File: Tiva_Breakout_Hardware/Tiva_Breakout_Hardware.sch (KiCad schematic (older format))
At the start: 54 parts, among them U1 TM4C129E_Launchpad

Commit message: Finished all wiring and LEDs, need resizing and silkscreen
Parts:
- gave numbers to parts that had none: 20
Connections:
- net PATCH10_EN: now also ConnPCH_C2.2 (Pin_2), R15.2, U1.PF1 (C1_1); no longer ConnPCH_C2.1 (Pin_1), R24.2, U1.PL3 (C1_10)
- net PATCH1_EN: now also ConnPCH_C2.1 (Pin_1), R24.2, U1.PL3 (C1_10); no longer ConnPCH_C2.2 (Pin_2), R15.2, U1.PF1 (C1_1)
- net PATCH2_EN: now also ConnPCH_C2.3 (Pin_3), R23.2, U1.PL2 (C1_9); no longer ConnPCH_C2.4 (Pin_4), R16.2, U1.PF2 (C1_2)
- net PATCH3_EN: now also ConnPCH_C2.5 (Pin_5), R22.2, U1.PL1 (C1_8); no longer ConnPCH_C2.6 (Pin_6), R17.2, U1.PF3 (C1_3)
- net PATCH4_EN: now also ConnPCH_C2.7 (Pin_7), R21.2, U1.PL0 (C1_7); no longer ConnPCH_C2.8 (Pin_8), R18.2, U1.PG0 (C1_4)
- net PATCH5_EN: now also ConnPCH_C2.9 (Pin_9), R20.2, U1.PL5 (C1_6); no longer ConnPCH_C2.10 (Pin_10), R19.2, U1.PL4 (C1_5)
- net PATCH6_EN: now also ConnPCH_C2.10 (Pin_10), R19.2, U1.PL4 (C1_5); no longer ConnPCH_C2.9 (Pin_9), R20.2, U1.PL5 (C1_6)
- net PATCH7_EN: now also ConnPCH_C2.8 (Pin_8), R18.2, U1.PG0 (C1_4); no longer ConnPCH_C2.7 (Pin_7), R21.2, U1.PL0 (C1_7)
- net PATCH8_EN: now also ConnPCH_C2.6 (Pin_6), R17.2, U1.PF3 (C1_3); no longer ConnPCH_C2.5 (Pin_5), R22.2, U1.PL1 (C1_8)
- net PATCH9_EN: now also ConnPCH_C2.4 (Pin_4), R16.2, U1.PF2 (C1_2); no longer ConnPCH_C2.3 (Pin_3), R23.2, U1.PL2 (C1_9)

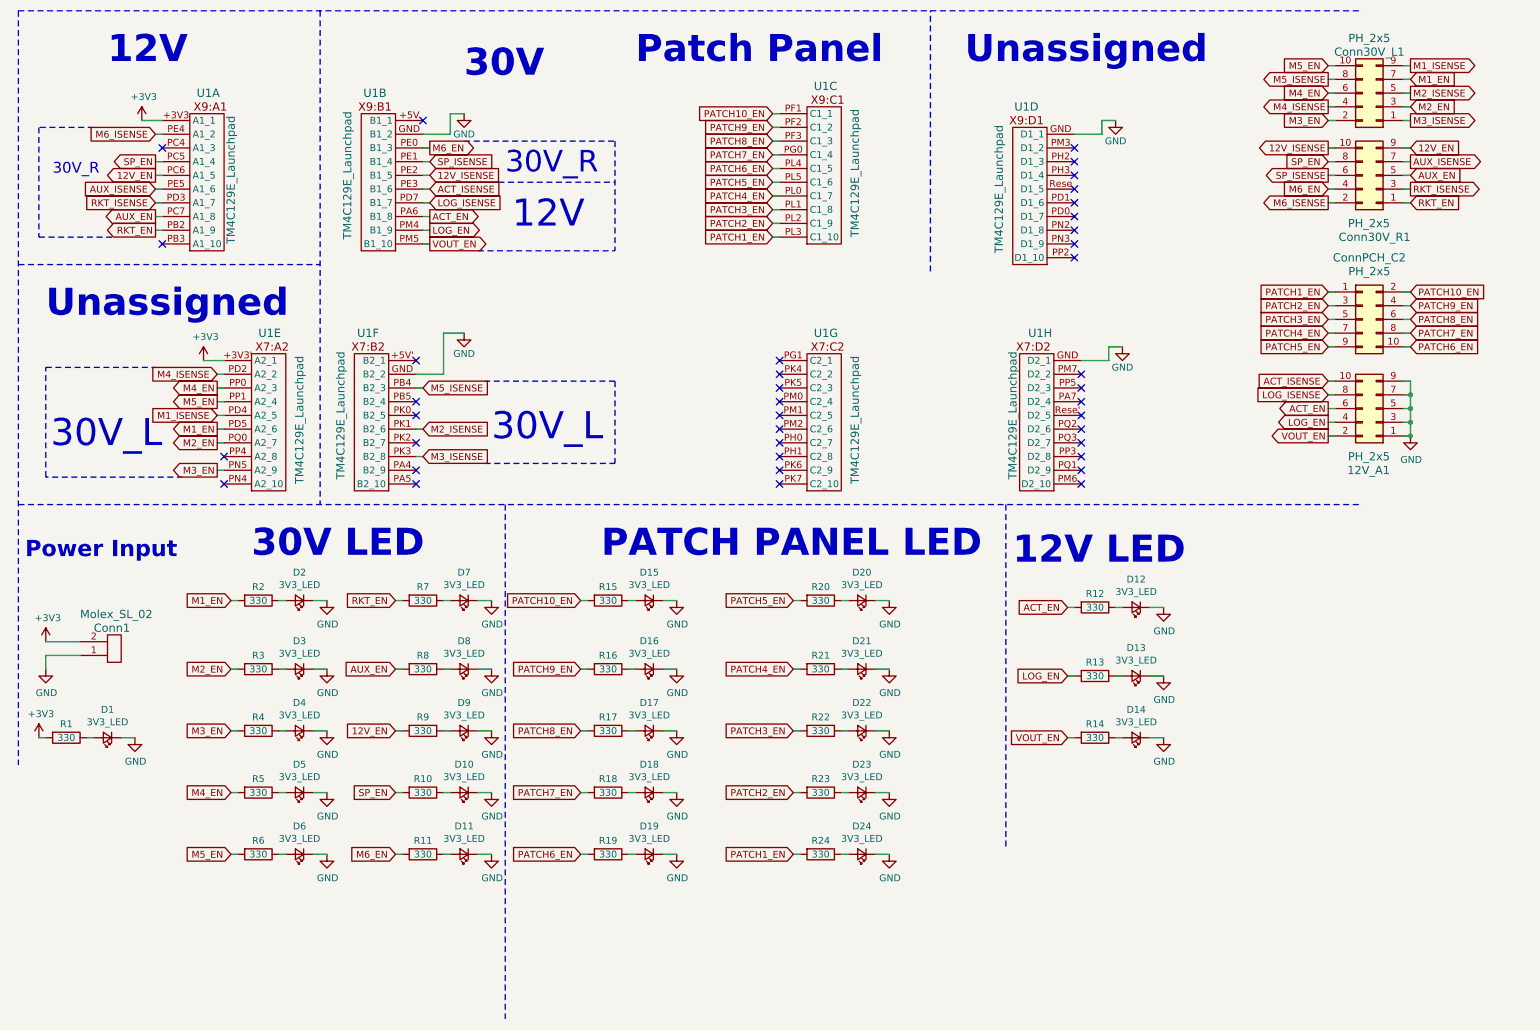
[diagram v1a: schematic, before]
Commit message: Finished layout, minus some silk screen stuff
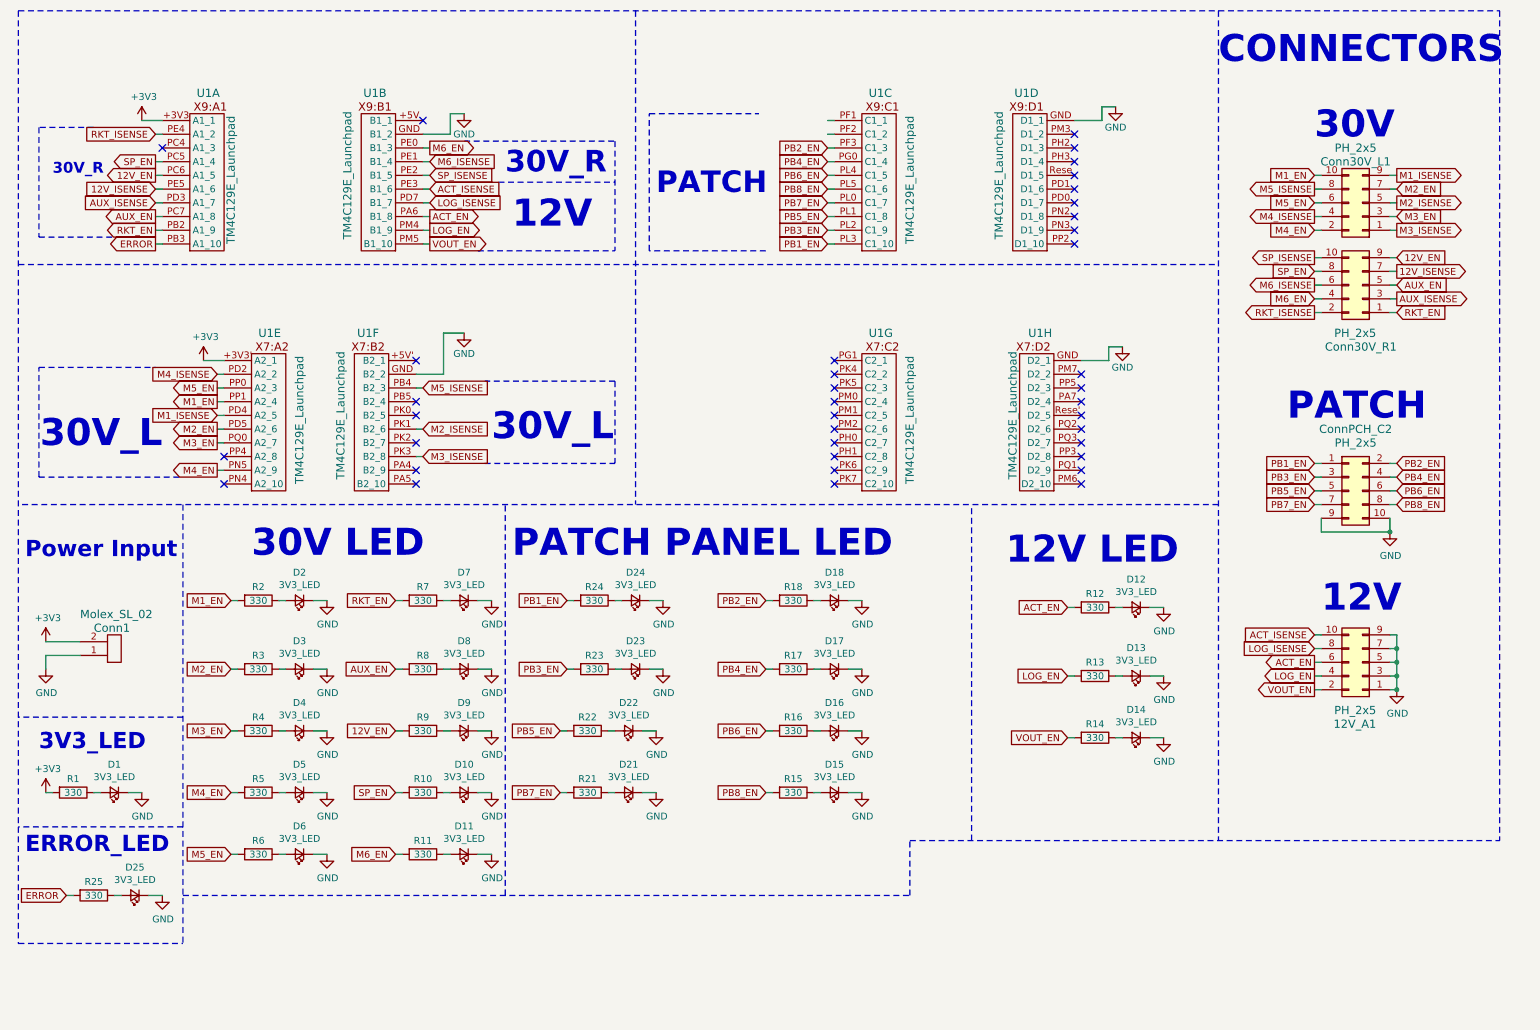
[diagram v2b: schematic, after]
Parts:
- removed D19, D20: 3V3_LED, LED_SMD:LED_0603_1608Metric_Pad1.05x0.95mm_HandSolder, symbol Device:LED_Small
- removed R19, R20: 330, Resistor_SMD:R_0603_1608Metric_Pad1.05x0.95mm_HandSolder, symbol Device:R
- added D25: 3V3_LED, LED_SMD:LED_0603_1608Metric_Pad1.05x0.95mm_HandSolder, symbol Device:LED_Small
- added R25: 330, Resistor_SMD:R_0603_1608Metric_Pad1.05x0.95mm_HandSolder, symbol Device:R
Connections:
- net 12V_ISENSE: now also Conn30V_R1.7 (Pin_7), U1.PE5 (A1_6); no longer Conn30V_R1.10 (Pin_10), U1.PE2 (B1_5)
- net AUX_ISENSE: now also Conn30V_R1.3 (Pin_3), U1.PD3 (A1_7); no longer Conn30V_R1.7 (Pin_7), U1.PE5 (A1_6)
- net GND: now also ConnPCH_C2.10 (Pin_10), ConnPCH_C2.9 (Pin_9), D25.1 (K)
- net M1_EN: now also Conn30V_L1.10 (Pin_10), U1.PP1 (A2_4); no longer Conn30V_L1.7 (Pin_7), U1.PD5 (A2_6)
- net M2_EN: now also Conn30V_L1.7 (Pin_7), U1.PD5 (A2_6); no longer Conn30V_L1.3 (Pin_3), U1.PQ0 (A2_7)
- net M3_EN: now also Conn30V_L1.3 (Pin_3), U1.PQ0 (A2_7); no longer Conn30V_L1.2 (Pin_2), U1.PN5 (A2_9)
- net M4_EN: now also Conn30V_L1.2 (Pin_2), U1.PN5 (A2_9); no longer Conn30V_L1.6 (Pin_6), U1.PP0 (A2_3)
- net M5_EN: now also Conn30V_L1.6 (Pin_6), U1.PP0 (A2_3); no longer Conn30V_L1.10 (Pin_10), U1.PP1 (A2_4)
- net M6_ISENSE: now also Conn30V_R1.6 (Pin_6), U1.PE1 (B1_4); no longer Conn30V_R1.2 (Pin_2), U1.PE4 (A1_2)
- net RKT_ISENSE: now also Conn30V_R1.2 (Pin_2), U1.PE4 (A1_2); no longer Conn30V_R1.3 (Pin_3), U1.PD3 (A1_7)
- net SP_ISENSE: now also Conn30V_R1.10 (Pin_10), U1.PE2 (B1_5); no longer Conn30V_R1.6 (Pin_6), U1.PE1 (B1_4)
- net ERROR: now reaches U1.PB3 (A1_10)
- net ERROR: now also R25.2
- removed net PATCH10_EN: ConnPCH_C2.2 (Pin_2), R15.2, U1.PF1 (C1_1)
- net PATCH1_EN renamed PB1_EN
- net PATCH2_EN renamed PB3_EN
- net PATCH3_EN renamed PB5_EN
- net PATCH4_EN renamed PB7_EN
- net PATCH5_EN renamed PB8_EN
- net PB8_EN: now also ConnPCH_C2.8 (Pin_8), R15.2; no longer ConnPCH_C2.9 (Pin_9)
- net PATCH6_EN renamed PB6_EN
- net PB6_EN: now also ConnPCH_C2.6 (Pin_6), R16.2; no longer ConnPCH_C2.10 (Pin_10)
- removed net PATCH7_EN: ConnPCH_C2.8 (Pin_8), R18.2, U1.PG0 (C1_4)
- removed net PATCH8_EN: ConnPCH_C2.6 (Pin_6), R17.2, U1.PF3 (C1_3)
- removed net PATCH9_EN: ConnPCH_C2.4 (Pin_4), R16.2, U1.PF2 (C1_2)
- new net: D25.2 (A), R25.1
- new net PB2_EN: ConnPCH_C2.2 (Pin_2), R18.2, U1.PF3 (C1_3)
- new net PB4_EN: ConnPCH_C2.4 (Pin_4), R17.2, U1.PG0 (C1_4)
- no-connect marks 39 -> 38
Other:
- note added: "3V3_LED"
- note added: "CONNECTORS"
- note added: "ERROR_LED"
- note added: "PATCH"
- note removed: "Patch Panel"
- note removed: "Unassigned"
- moved on the sheet: 12V_A1, Conn30V_L1, Conn30V_R1, ConnPCH_C2, D1, D15, D16, D17, D18, D21, D22, D23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

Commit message: Added pulldown resistors & LED colors
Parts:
- added R19, R20, R26, R27, R28, R29, R30, R31: 10k, Resistor_SMD:R_0603_1608Metric_Pad1.05x0.95mm_HandSolder, symbol Device:R
- D1: value 3V3_LED -> GRN
- D10, D11, D12, D13, D14, D15, D16, D17, D18, D2, D21, D22, D23, D24, D3, D4, D5, D6, D7, D8, D9: value 3V3_LED -> BLU
- D25: value 3V3_LED -> RED
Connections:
- net GND: now also R19.1, R20.1, R26.1, R27.1, R28.1, R29.1, R30.1, R31.1
- net PB1_EN: now also R19.2
- net PB2_EN: now also R28.2
- net PB3_EN: now also R20.2
- net PB4_EN: now also R29.2
- net PB5_EN: now also R26.2
- net PB6_EN: now also R30.2
- net PB7_EN: now also R27.2
- net PB8_EN: now also R31.2
- no-connect marks 38 -> 40
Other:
- note added: "PATCH PANEL LED/PULLDOWN"
- note removed: "PATCH PANEL LED"
- moved on the sheet: D15, D16, D17, D21, D22, D23, R15, R16, R17, R21, R22, R23

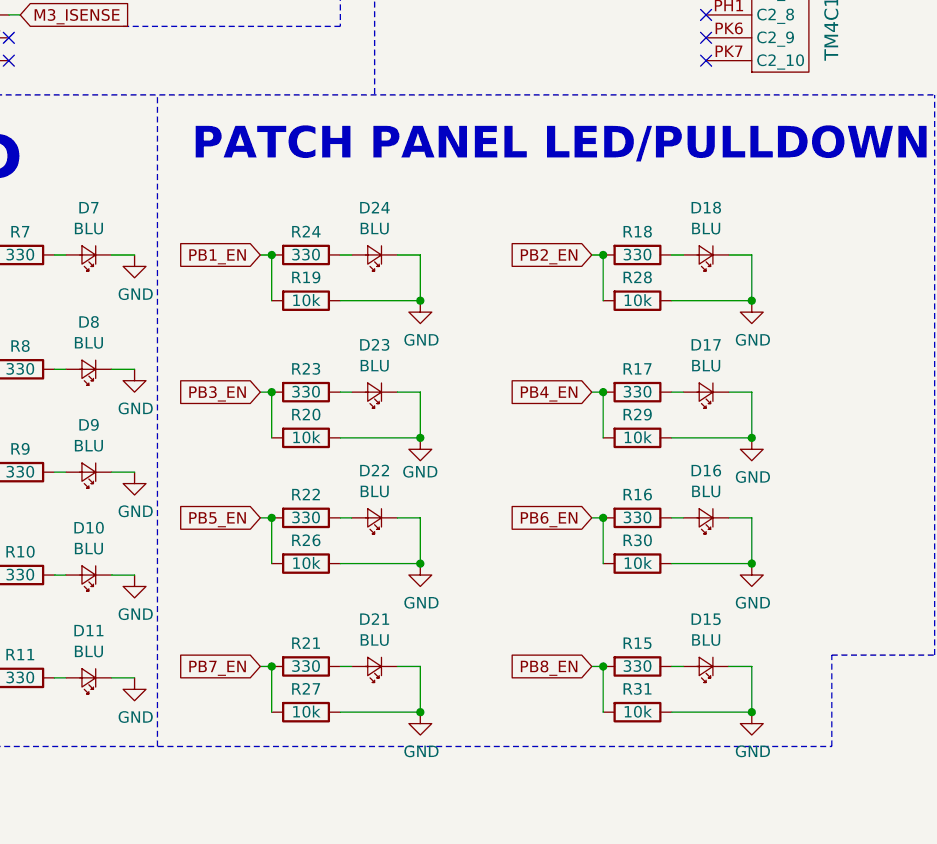
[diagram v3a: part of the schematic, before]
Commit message: Added pullup resistors and pin labels
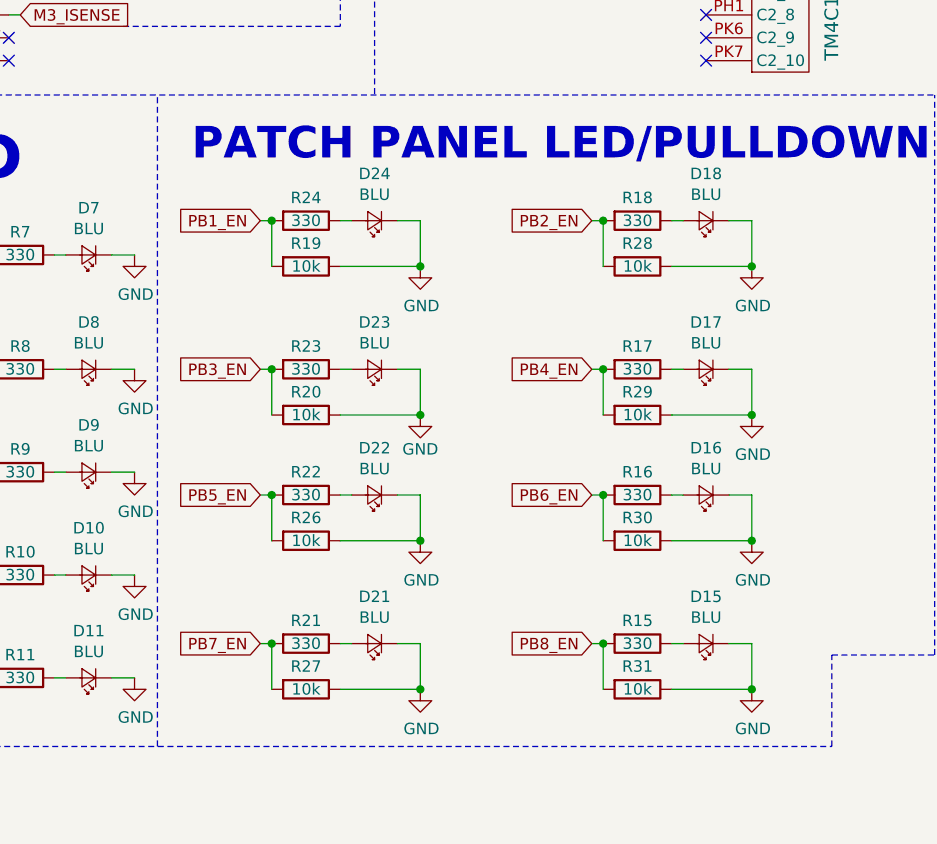
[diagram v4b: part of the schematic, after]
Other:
- moved on the sheet: D15, D16, D17, D18, D21, D22, D23, D24, R15, R16, R17, R18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
